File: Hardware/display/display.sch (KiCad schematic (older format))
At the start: 5 parts, among them J1 CONN_01X08, J2 CONN_01X08

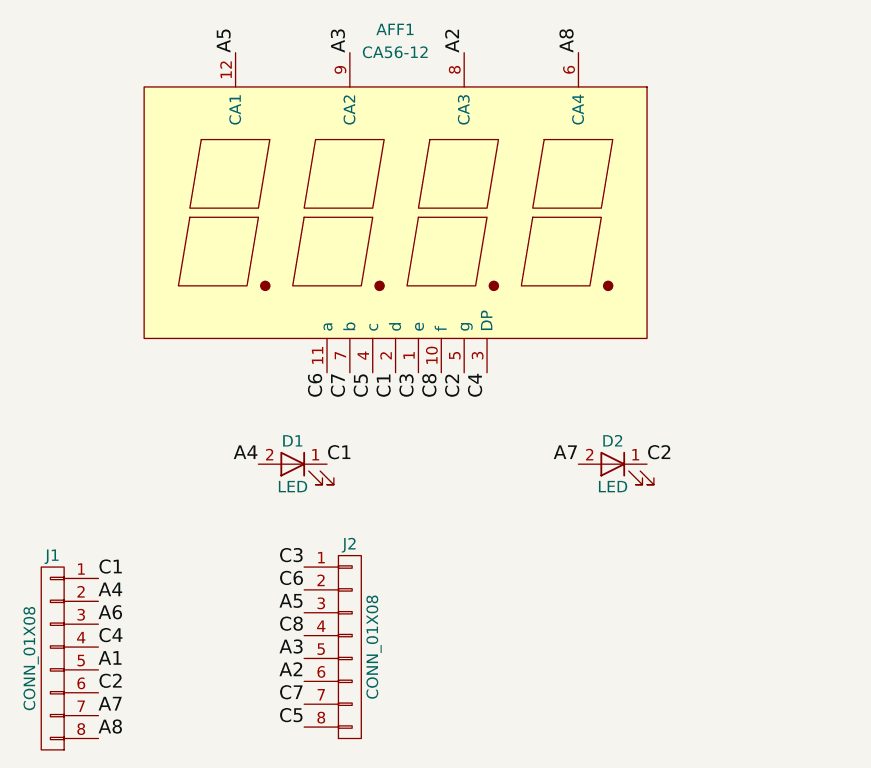
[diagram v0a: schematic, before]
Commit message: Added 2 more LEDs
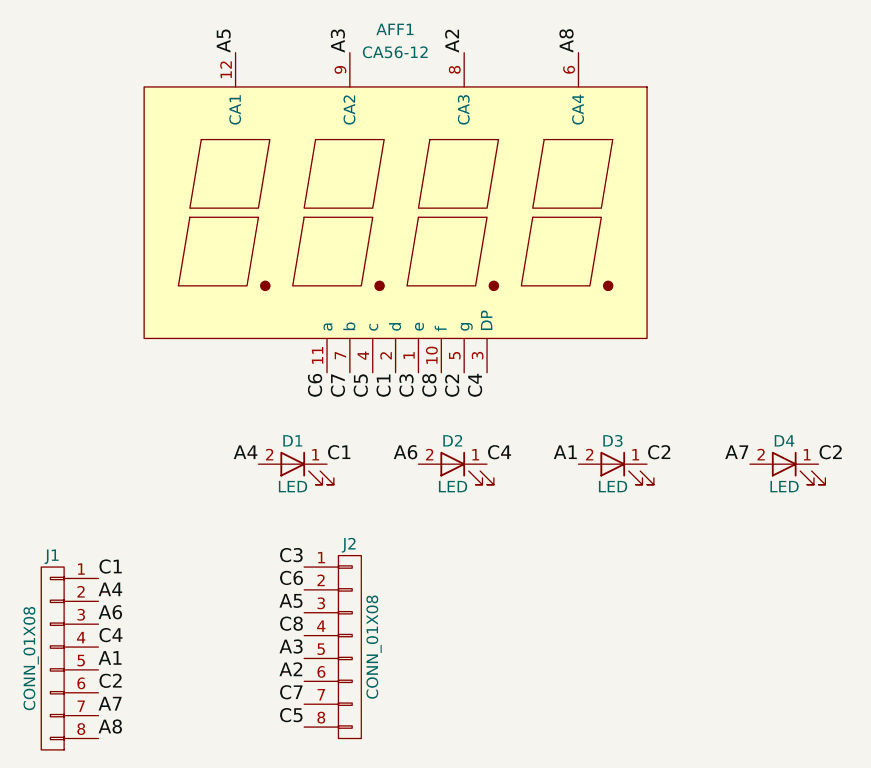
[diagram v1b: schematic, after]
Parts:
- added D2, D4: LED, LEDs:LED_D5.0mm, symbol LED
- renumbered D2 to D3
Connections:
- net A1: now also D3.2 (A)
- net A6: now also D2.2 (A)
- net A7: now also D4.2 (A); no longer D3.2 (A)
- net C2: now also D4.1 (K)
- net C4: now also D2.1 (K)
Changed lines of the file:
@@
 LIBS:valves
 LIBS:my_display
+LIBS:display-cache
 EELAYER 25 0
 EELAYER END
@@
 $EndComp
 $Comp
-L LED D2
+L LED D3
 U 1 1 59A2E1E5
 P 6650 3050
-F 0 "D2" H 6650 3150 50  0000 C CNN
+F 0 "D3" H 6650 3150 50  0000 C CNN
 F 1 "LED" H 6650 2950 50  0000 C CNN
 F 2 "LEDs:LED_D5.0mm" H 6650 3050 50  0001 C CNN
@@
 A4
 Text Label 6500 3050 2    60   ~ 0
-A7
+A1
 Text Label 5400 3050 0    60   ~ 0
 C1
 Text Label 6800 3050 0    60   ~ 0
 C2
+$Comp
+L LED D2
+U 1 1 59D0F748
+P 5950 3050
+F 0 "D2" H 5950 3150 50  0000 C CNN
+F 1 "LED" H 5950 2950 50  0000 C CNN
+F 2 "LEDs:LED_D5.0mm" H 5950 3050 50  0001 C CNN
+F 3 "" H 5950 3050 50  0001 C CNN
+	1    5950 3050
+	-1   0    0    -1
+$EndComp
+Text Label 5800 3050 2    60   ~ 0
+A6
+Text Label 6100 3050 0    60   ~ 0
+C4
+$Comp
+L LED D4
+U 1 1 59D0F800
+P 7400 3050
+F 0 "D4" H 7400 3150 50  0000 C CNN
+F 1 "LED" H 7400 2950 50  0000 C CNN
+F 2 "LEDs:LED_D5.0mm" H 7400 3050 50  0001 C CNN
+F 3 "" H 7400 3050 50  0001 C CNN
+	1    7400 3050
+	-1   0    0    -1
+$EndComp
+Text Label 7250 3050 2    60   ~ 0
+A7
+Text Label 7550 3050 0    60   ~ 0
+C2
 $EndSCHEMATC
